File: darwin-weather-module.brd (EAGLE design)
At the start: 85 x 25 mm, 14 parts, among them U1 P82B715SOIC

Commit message: Schematic Cleanup
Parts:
- renumbered U$1 to J1, U$2 to U2, U$3 to U3, U$5 to J2
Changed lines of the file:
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@@
 </autorouter>
 <elements>
-<element name="U$1" library="Conservify" library_urn="urn:adsk.eagle:library:11839183" package="M20-7810645" package3d_urn="urn:adsk.eagle:package:11839232/3" value="2X6-HEADERS" x="7.5" y="12.5" smashed="yes" rot="R90"/>
-<element name="U$2" library="Conservify" library_urn="urn:adsk.eagle:library:11839183" package="QFN50P400X400X100-25T200" package3d_urn="urn:adsk.eagle:package:12019890/1" value="ATSAMD09" x="22" y="11" smashed="yes" rot="R270"/>
+<element name="J1" library="Conservify" library_urn="urn:adsk.eagle:library:11839183" package="M20-7810645" package3d_urn="urn:adsk.eagle:package:11839232/3" value="2X6-HEADERS" x="7.5" y="12.5" smashed="yes" rot="R90"/>
+<element name="U2" library="Conservify" library_urn="urn:adsk.eagle:library:11839183" package="QFN50P400X400X100-25T200" package3d_urn="urn:adsk.eagle:package:12019890/1" value="ATSAMD09" x="22" y="11" smashed="yes" rot="R270"/>
 <element name="U1" library="Conservify" library_urn="urn:adsk.eagle:library:11839183" package="SOIC127P599X175-8" package3d_urn="urn:adsk.eagle:package:11891718/1" value="P82B715SOIC" x="22" y="5" smashed="yes">
 <attribute name="NAME" x="22" y="8.5949" size="1.27" layer="25" align="bottom-center"/>
@@
 <attribute name="VALUE" x="26.9" y="17.6" size="0.4064" layer="27" ratio="10"/>
 </element>
-<element name="U$3" library="Conservify" library_urn="urn:adsk.eagle:library:11839183" package="SOIC127P600X175-8" package3d_urn="urn:adsk.eagle:package:12022475/1" value="M24C02-WMN6TP" x="15" y="5" smashed="yes" rot="R270"/>
-<element name="U$5" library="Conservify" library_urn="urn:adsk.eagle:library:11839183" package="85513-5009" package3d_urn="urn:adsk.eagle:package:12024212/2" value="95501-6889VERT" x="73" y="5" smashed="yes"/>
+<element name="U3" library="Conservify" library_urn="urn:adsk.eagle:library:11839183" package="SOIC127P600X175-8" package3d_urn="urn:adsk.eagle:package:12022475/1" value="M24C02-WMN6TP" x="15" y="5" smashed="yes" rot="R270"/>
+<element name="J2" library="Conservify" library_urn="urn:adsk.eagle:library:11839183" package="85513-5009" package3d_urn="urn:adsk.eagle:package:12024212/2" value="95501-6889VERT" x="73" y="5" smashed="yes"/>
 <element name="C1" library="rcl" library_urn="urn:adsk.eagle:library:334" package="C0603K" package3d_urn="urn:adsk.eagle:package:23680/2" value=".1uf" x="19" y="1.6" smashed="yes">
 <attribute name="NAME" x="20.867" y="1.107" size="1" layer="25" ratio="30"/>
@@
 <contactref element="X1" pad="5"/>
 <contactref element="X1" pad="9"/>
-<contactref element="U$2" pad="23"/>
+<contactref element="U2" pad="23"/>
 <contactref element="U1" pad="4"/>
 <wire x1="22.175" y1="18" x2="22.325" y2="18.15" width="0.1524" layer="1"/>
 <wire x1="22.325" y1="18.15" x2="24" y2="18.15" width="0.1524" layer="1"/>
-<contactref element="U$3" pad="1"/>
-<contactref element="U$3" pad="2"/>
-<contactref element="U$3" pad="3"/>
-<contactref element="U$3" pad="4"/>
+<contactref element="U3" pad="1"/>
+<contactref element="U3" pad="2"/>
+<contactref element="U3" pad="3"/>
+<contactref element="U3" pad="4"/>
 <polygon width="0.1524" layer="1">
 <vertex x="0" y="25"/>
@@
 <vertex x="0" y="0"/>
 </polygon>
-<contactref element="U$1" pad="P$8"/>
-<contactref element="U$5" pad="3"/>
-<contactref element="U$5" pad="2"/>
-<contactref element="U$5" pad="1"/>
+<contactref element="J1" pad="P$8"/>
+<contactref element="J2" pad="3"/>
+<contactref element="J2" pad="2"/>
+<contactref element="J2" pad="1"/>
 <polygon width="0.4064" layer="16">
 <vertex x="0" y="25"/>
@@
 <contactref element="C9" pad="1"/>
 <contactref element="X1" pad="1"/>
-<contactref element="U$2" pad="24"/>
+<contactref element="U2" pad="24"/>
 <contactref element="U1" pad="8"/>
 <wire x1="19.825" y1="17.05" x2="18.169" y2="17.05" width="0.1524" layer="1"/>
@@
 <wire x1="30.48" y1="15.875" x2="30.46" y2="15.895" width="0.1524" layer="1"/>
 <wire x1="30.46" y1="15.895" x2="30.46" y2="18.05" width="0.1524" layer="1"/>
-<contactref element="U$3" pad="8"/>
+<contactref element="U3" pad="8"/>
 <wire x1="26" y1="3.088459375" x2="26" y2="7" width="0.1524" layer="1"/>
 <wire x1="25.438140625" y1="2.5266" x2="26" y2="3.088459375" width="0.1524" layer="1"/>
@@
 <signal name="UNREG">
 <contactref element="U$4" pad="1"/>
-<contactref element="U$1" pad="P$7"/>
+<contactref element="J1" pad="P$7"/>
 <wire x1="4.59" y1="18.85" x2="4.59" y2="20.59" width="0.4064" layer="1"/>
 <wire x1="4.59" y1="20.59" x2="6" y2="22" width="0.4064" layer="1"/>
@@
 <wire x1="25" y1="16" x2="23.225" y2="16" width="0.4064" layer="1"/>
 <wire x1="23.225" y1="16" x2="22.175" y2="17.05" width="0.4064" layer="1"/>
-<contactref element="U$5" pad="4"/>
-<contactref element="U$5" pad="5"/>
-<contactref element="U$5" pad="6"/>
+<contactref element="J2" pad="4"/>
+<contactref element="J2" pad="5"/>
+<contactref element="J2" pad="6"/>
 <wire x1="24" y1="22" x2="28.42710625" y2="22" width="0.4064" layer="1"/>
 <wire x1="28.42710625" y1="22" x2="29.93270625" y2="23.5056" width="0.4064" layer="1"/>
@@
 <signal name="SWCLK">
 <contactref element="X1" pad="4"/>
-<contactref element="U$2" pad="19"/>
+<contactref element="U2" pad="19"/>
 <wire x1="31.73" y1="21.27" x2="31.73" y2="21.95" width="0.1524" layer="1"/>
 <wire x1="29.004271875" y1="18.544271875" x2="31.73" y2="21.27" width="0.1524" layer="1"/>
@@
 <signal name="SWDIO">
 <contactref element="X1" pad="2"/>
-<contactref element="U$2" pad="20"/>
+<contactref element="U2" pad="20"/>
 <wire x1="27.469375" y1="18.959375" x2="30.46" y2="21.95" width="0.1524" layer="1"/>
 <wire x1="27.469375" y1="13.484196875" x2="27.469375" y2="18.959375" width="0.1524" layer="1"/>
@@
 <signal name="RESET">
 <contactref element="X1" pad="10"/>
-<contactref element="U$2" pad="18"/>
+<contactref element="U2" pad="18"/>
 <wire x1="35.54" y1="21.27" x2="35.54" y2="21.95" width="0.1524" layer="1"/>
 <wire x1="33.635" y1="19.365" x2="35.54" y2="21.27" width="0.1524" layer="1"/>
@@
 </signal>
 <signal name="SDA">
-<contactref element="U$2" pad="11"/>
-<contactref element="U$3" pad="5"/>
+<contactref element="U2" pad="11"/>
+<contactref element="U3" pad="5"/>
 <wire x1="19.764834375" y1="10.25" x2="20.0627" y2="10.25" width="0.1524" layer="1"/>
 <wire x1="17.8350375" y1="8.320203125" x2="19.764834375" y2="10.25" width="0.1524" layer="1"/>
@@
 <wire x1="13.095" y1="2.782034375" x2="15.312965625" y2="5" width="0.1524" layer="1"/>
 <wire x1="13.095" y1="2.5266" x2="13.095" y2="2.782034375" width="0.1524" layer="1"/>
-<contactref element="U$1" pad="P$3"/>
+<contactref element="J1" pad="P$3"/>
 <wire x1="10.41" y1="11.23" x2="12.58185" y2="9.05815" width="0.1524" layer="1"/>
 <wire x1="13.095" y1="5.9479875" x2="13.095" y2="2.5266" width="0.1524" layer="1"/>
@@
 </signal>
 <signal name="SCL">
-<contactref element="U$2" pad="12"/>
-<contactref element="U$3" pad="6"/>
+<contactref element="U2" pad="12"/>
+<contactref element="U3" pad="6"/>
 <wire x1="18.19111875" y1="7.87841875" x2="20.0627" y2="9.75" width="0.1524" layer="1"/>
 <wire x1="18.19111875" y1="6.759465625" x2="18.19111875" y2="7.87841875" width="0.1524" layer="1"/>
 <wire x1="14.365" y1="2.933346875" x2="18.19111875" y2="6.759465625" width="0.1524" layer="1"/>
 <wire x1="14.365" y1="2.5266" x2="14.365" y2="2.933346875" width="0.1524" layer="1"/>
-<contactref element="U$1" pad="P$2"/>
+<contactref element="J1" pad="P$2"/>
 <wire x1="10.41" y1="8.69" x2="12.27705" y2="6.82295" width="0.1524" layer="1"/>
 <wire x1="13" y1="1.0961875" x2="13" y2="1.0922" width="0.1524" layer="1"/>
@@
 </signal>
 <signal name="SENSE-SDA">
-<contactref element="U$2" pad="15"/>
+<contactref element="U2" pad="15"/>
 <contactref element="U1" pad="3"/>
 <wire x1="19.5299" y1="4.365" x2="20.796340625" y2="4.365" width="0.1524" layer="1"/>
@@
 </signal>
 <signal name="SENSE-SCL">
-<contactref element="U$2" pad="16"/>
+<contactref element="U2" pad="16"/>
 <contactref element="U1" pad="6"/>
 <wire x1="24.4701" y1="4.365" x2="23.203659375" y2="4.365" width="0.1524" layer="1"/>
@@
 </signal>
 <signal name="WC">
-<contactref element="U$2" pad="13"/>
-<contactref element="U$3" pad="7"/>
+<contactref element="U2" pad="13"/>
+<contactref element="U3" pad="7"/>
 <wire x1="20.75" y1="6.588659375" x2="20.75" y2="9.0627" width="0.1524" layer="1"/>
 <wire x1="20.4737875" y1="6.312446875" x2="20.75" y2="6.588659375" width="0.1524" layer="1"/>
@@
 </signal>
 <signal name="NC">
-<contactref element="U$1" pad="P$1"/>
+<contactref element="J1" pad="P$1"/>
 </signal>
 <signal name="MISO">
-<contactref element="U$1" pad="P$4"/>
+<contactref element="J1" pad="P$4"/>
 </signal>
 <signal name="MOSI">
-<contactref element="U$1" pad="P$5"/>
+<contactref element="J1" pad="P$5"/>
 </signal>
 <signal name="SCK">
-<contactref element="U$1" pad="P$6"/>
+<contactref element="J1" pad="P$6"/>
 </signal>
 <signal name="ENABLE">
-<contactref element="U$1" pad="P$10"/>
+<contactref element="J1" pad="P$10"/>
 <contactref element="U$4" pad="3"/>
 <contactref element="R1" pad="2"/>
@@
 </signal>
 <signal name="G1">
-<contactref element="U$1" pad="P$11"/>
+<contactref element="J1" pad="P$11"/>
 </signal>
 <signal name="G2">
-<contactref element="U$1" pad="P$12"/>
+<contactref element="J1" pad="P$12"/>
 </signal>
 <signal name="IN3V3">
-<contactref element="U$1" pad="P$9"/>
+<contactref element="J1" pad="P$9"/>
 </signal>
 <signal name="LCL">
-<contactref element="U$5" pad="7"/>
+<contactref element="J2" pad="7"/>
 <contactref element="U1" pad="7"/>
 <wire x1="24.4701" y1="5.635" x2="23.6068" y2="5.635" width="0.1524" layer="1"/>
@@
 </signal>
 <signal name="LDA">
-<contactref element="U$5" pad="8"/>
+<contactref element="J2" pad="8"/>
 <contactref element="U1" pad="2"/>
 <wire x1="19.5299" y1="5.635" x2="21.127" y2="5.635" width="0.1524" layer="1"/>

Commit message: Added I2C Pullups and GPIO connection to backplane. Removed deprecated module mounting hole.
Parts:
- added R2, R3: 4.7k, SparkFun-Resistors:0603
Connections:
- net 3V3: now also R2.1, R3.1
- net G1: now also U2.22
- net SCL: now also R3.2
- net SDA: now also R2.2
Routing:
- net G1: track 0.00 -> 32.3 mm, vias 0 -> 2
- net 3V3: track 49.8 -> 68.1 mm, vias 3 -> 5
- net SDA: track 21.0 -> 23.3 mm
- net GND: track 1.89 -> 3.30 mm
- net SCL: track 20.8 -> 22.1 mm
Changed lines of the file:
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@@
 <attribute name="SPICEPREFIX" value="C" x="25.4" y="14.4" size="1.778" layer="27" display="off"/>
+</element>
+<element name="R2" library="SparkFun-Resistors" library_urn="urn:adsk.eagle:library:532" package="0603" package3d_urn="urn:adsk.eagle:package:39650/1" value="4.7k" x="13.6" y="11.2" smashed="yes" rot="R180">
+<attribute name="NAME" x="13.6" y="10.438" size="0.6096" layer="25" font="vector" ratio="20" rot="R180" align="bottom-center"/>
+<attribute name="PROD_ID" value="RES-07828" x="13.6" y="11.2" size="1.778" layer="27" rot="R180" display="off"/>
+<attribute name="VALUE" x="13.6" y="11.962" size="0.6096" layer="27" font="vector" ratio="20" rot="R180" align="top-center"/>
+</element>
+<element name="R3" library="SparkFun-Resistors" library_urn="urn:adsk.eagle:library:532" package="0603" package3d_urn="urn:adsk.eagle:package:39650/1" value="4.7k" x="10.4" y="2.4" smashed="yes">
+<attribute name="NAME" x="10.4" y="3.162" size="0.6096" layer="25" font="vector" ratio="20" align="bottom-center"/>
+<attribute name="PROD_ID" value="RES-07828" x="10.4" y="2.4" size="1.778" layer="27" display="off"/>
+<attribute name="VALUE" x="10.4" y="1.638" size="0.6096" layer="27" font="vector" ratio="20" align="top-center"/>
 </element>
 </elements>
 <signals>
 <signal name="N$1">
-<via x="33.5" y="12.5" extent="1-16" drill="4.2" diameter="6"/>
 <via x="58.5" y="12.5" extent="1-16" drill="4.2" diameter="6"/>
-<wire x1="33.5" y1="12.5" x2="58.5" y2="12.5" width="0" layer="19" extent="1-1"/>
 </signal>
 <signal name="GND">
@@
 <via x="25.2" y="1.6" extent="1-16" drill="0.35"/>
 <via x="26.2" y="1.6" extent="1-16" drill="0.35"/>
+<wire x1="24.48515625" y1="11.8" x2="23.9873" y2="11.8" width="0.1524" layer="1"/>
+<wire x1="23.9373" y1="11.75" x2="23.9873" y2="11.8" width="0.1524" layer="1"/>
+<wire x1="24.48515625" y1="11.8" x2="24.6" y2="11.91484375" width="0.1524" layer="1"/>
+<wire x1="24.6" y1="11.91484375" x2="24.6" y2="12.6" width="0.1524" layer="1"/>
 </signal>
 <signal name="3V3">
@@
 <wire x1="24.5651" y1="7" x2="26" y2="7" width="0.1524" layer="1"/>
 <via x="26" y="7" extent="1-16" drill="0.35"/>
-<wire x1="26" y1="7" x2="22" y2="11" width="0.1524" layer="16"/>
-<wire x1="22" y1="11" x2="22" y2="15" width="0.1524" layer="16"/>
+<wire x1="26" y1="12.4" x2="26" y2="7" width="0.1524" layer="16"/>
+<wire x1="26" y1="12.4" x2="23.4" y2="15" width="0.1524" layer="16"/>
+<wire x1="23.4" y1="15" x2="22" y2="15" width="0.1524" layer="16"/>
 <via x="22" y="15" extent="1-16" drill="0.35"/>
 <wire x1="22" y1="15" x2="22.875" y2="15.875" width="0.1524" layer="16"/>
@@
 <wire x1="26" y1="3.088459375" x2="26" y2="7" width="0.1524" layer="1"/>
 <wire x1="25.438140625" y1="2.5266" x2="26" y2="3.088459375" width="0.1524" layer="1"/>
-<wire x1="16.905" y1="2.5266" x2="17" y2="2.5266" width="0.1524" layer="1"/>
 <contactref element="C2" pad="1"/>
 <contactref element="C1" pad="1"/>
 <contactref element="C3" pad="1"/>
-<wire x1="17.1984" y1="2.5266" x2="25.438140625" y2="2.5266" width="0.1524" layer="1"/>
+<wire x1="17.1984" y1="2.5266" x2="18" y2="2.5266" width="0.1524" layer="1"/>
+<wire x1="18" y1="2.5266" x2="25.438140625" y2="2.5266" width="0.1524" layer="1"/>
 <wire x1="24.525" y1="14.4" x2="23.9373" y2="13.8123" width="0.1524" layer="1"/>
 <wire x1="23.9373" y1="13.8123" x2="23.9373" y2="13.0627" width="0.1524" layer="1"/>
@@
 <wire x1="27.125" y1="7" x2="26" y2="7" width="0.1524" layer="1"/>
 <wire x1="18.125" y1="1.6" x2="17.1984" y2="2.5266" width="0.1524" layer="1"/>
-<wire x1="17.1984" y1="2.5266" x2="17" y2="2.5266" width="0.1524" layer="1"/>
+<wire x1="17.1984" y1="2.5266" x2="16.905" y2="2.5266" width="0.1524" layer="1"/>
+<contactref element="R3" pad="1"/>
+<contactref element="R2" pad="1"/>
+<wire x1="14.45" y1="11.2" x2="14.45" y2="14.518" width="0.1524" layer="1"/>
+<wire x1="14.45" y1="14.518" x2="16.539" y2="16.607" width="0.1524" layer="1"/>
+<wire x1="9.55" y1="2.4" x2="8.2" y2="2.4" width="0.1524" layer="1"/>
+<via x="8.2" y="2.4" extent="1-16" drill="0.35"/>
+<wire x1="8.2" y1="2.4" x2="17.8734" y2="2.4" width="0.1524" layer="16"/>
+<wire x1="17.8734" y1="2.4" x2="18" y2="2.5266" width="0.1524" layer="16"/>
+<via x="18" y="2.5266" extent="1-16" drill="0.35"/>
 </signal>
 <signal name="N$6">
@@
 <wire x1="31.73" y1="21.27" x2="31.73" y2="21.95" width="0.1524" layer="1"/>
 <wire x1="29.004271875" y1="18.544271875" x2="31.73" y2="21.27" width="0.1524" layer="1"/>
-<wire x1="29.004271875" y1="14.51909375" x2="29.004271875" y2="18.544271875" width="0.1524" layer="1"/>
-<wire x1="24.235178125" y1="9.75" x2="29.004271875" y2="14.51909375" width="0.1524" layer="1"/>
-<wire x1="23.9373" y1="9.75" x2="24.235178125" y2="9.75" width="0.1524" layer="1"/>
+<wire x1="29.004271875" y1="14.11909375" x2="29.004271875" y2="18.544271875" width="0.1524" layer="1"/>
+<wire x1="24.635178125" y1="9.75" x2="29.004271875" y2="14.11909375" width="0.1524" layer="1"/>
+<wire x1="23.9373" y1="9.75" x2="24.635178125" y2="9.75" width="0.1524" layer="1"/>
 </signal>
 <signal name="SWDIO">
@@
 <contactref element="U2" pad="20"/>
 <wire x1="27.469375" y1="18.959375" x2="30.46" y2="21.95" width="0.1524" layer="1"/>
-<wire x1="27.469375" y1="13.484196875" x2="27.469375" y2="18.959375" width="0.1524" layer="1"/>
-<wire x1="24.235178125" y1="10.25" x2="27.469375" y2="13.484196875" width="0.1524" layer="1"/>
-<wire x1="23.9373" y1="10.25" x2="24.235178125" y2="10.25" width="0.1524" layer="1"/>
+<wire x1="27.469375" y1="13.084196875" x2="27.469375" y2="18.959375" width="0.1524" layer="1"/>
+<wire x1="24.635178125" y1="10.25" x2="27.469375" y2="13.084196875" width="0.1524" layer="1"/>
+<wire x1="23.9373" y1="10.25" x2="24.635178125" y2="10.25" width="0.1524" layer="1"/>
 </signal>
 <signal name="RESET">
@@
 <wire x1="13.095" y1="2.5266" x2="13.095" y2="2.782034375" width="0.1524" layer="1"/>
 <contactref element="J1" pad="P$3"/>
-<wire x1="10.41" y1="11.23" x2="12.58185" y2="9.05815" width="0.1524" layer="1"/>
 <wire x1="13.095" y1="5.9479875" x2="13.095" y2="2.5266" width="0.1524" layer="1"/>
 <wire x1="12.58185" y1="9.05815" x2="12.58185" y2="6.4611375" width="0.1524" layer="1"/>
 <wire x1="12.58185" y1="6.4611375" x2="13.095" y2="5.9479875" width="0.1524" layer="1"/>
+<contactref element="R2" pad="2"/>
+<wire x1="10.41" y1="11.23" x2="12.58185" y2="9.05815" width="0.1524" layer="1"/>
+<wire x1="10.41" y1="11.23" x2="12.72" y2="11.23" width="0.1524" layer="1"/>
+<wire x1="12.72" y1="11.23" x2="12.75" y2="11.2" width="0.1524" layer="1"/>
 </signal>
 <signal name="SCL">
@@
 <contactref element="J1" pad="P$2"/>
 <wire x1="10.41" y1="8.69" x2="12.27705" y2="6.82295" width="0.1524" layer="1"/>
-<wire x1="13" y1="1.0961875" x2="13" y2="1.0922" width="0.1524" layer="1"/>
-<wire x1="12.27705" y1="6.82295" x2="12.27705" y2="1.8191375" width="0.1524" layer="1"/>
-<wire x1="12.27705" y1="1.8191375" x2="13" y2="1.0961875" width="0.1524" layer="1"/>
-<wire x1="13" y1="1.0922" x2="14" y2="1.0922" width="0.1524" layer="1"/>
+<wire x1="12.6" y1="1.0961875" x2="12.6" y2="1.0922" width="0.1524" layer="1"/>
+<wire x1="12.27705" y1="6.82295" x2="12.27705" y2="2.4191375" width="0.1524" layer="1"/>
+<wire x1="12.27705" y1="2.4191375" x2="12.27705" y2="1.4191375" width="0.1524" layer="1"/>
+<wire x1="12.27705" y1="1.4191375" x2="12.6" y2="1.0961875" width="0.1524" layer="1"/>
+<wire x1="12.6" y1="1.0922" x2="14" y2="1.0922" width="0.1524" layer="1"/>
 <wire x1="14" y1="1.0922" x2="14.365" y2="1.4572" width="0.1524" layer="1"/>
 <wire x1="14.365" y1="1.4572" x2="14.365" y2="2.5266" width="0.1524" layer="1"/>
+<contactref element="R3" pad="2"/>
+<wire x1="11.25" y1="2.4" x2="12.2579125" y2="2.4" width="0.1524" layer="1"/>
+<wire x1="12.2579125" y1="2.4" x2="12.27705" y2="2.4191375" width="0.1524" layer="1"/>
 </signal>
 <signal name="SENSE-SDA">
@@
 <signal name="G1">
 <contactref element="J1" pad="P$11"/>
+<contactref element="U2" pad="22"/>
+<wire x1="4.59" y1="8.69" x2="3.09" y2="8.69" width="0.1524" layer="1"/>
+<wire x1="3.09" y1="8.69" x2="2.2" y2="7.8" width="0.1524" layer="1"/>
+<via x="2.2" y="7.8" extent="1-16" drill="0.35"/>
+<wire x1="2.2" y1="7.8" x2="2.31414375" y2="7.8" width="0.1524" layer="16"/>
+<wire x1="2.31414375" y1="7.8" x2="5.56634375" y2="4.5478" width="0.1524" layer="16"/>
+<wire x1="5.56634375" y1="4.5478" x2="18.1478" y2="4.5478" width="0.1524" layer="16"/>
+<wire x1="25.363515625" y1="11.763515625" x2="25.363515625" y2="12.0364875" width="0.1524" layer="16"/>
+<via x="25.363515625" y="12.0364875" extent="1-16" drill="0.35"/>
+<wire x1="25.363515625" y1="12.0364875" x2="24.577028125" y2="11.25" width="0.1524" layer="1"/>
+<wire x1="24.577028125" y1="11.25" x2="23.9373" y2="11.25" width="0.1524" layer="1"/>
+<wire x1="18.1478" y1="4.5478" x2="25.363515625" y2="11.763515625" width="0.1524" layer="16"/>
 </signal>
 <signal name="G2">

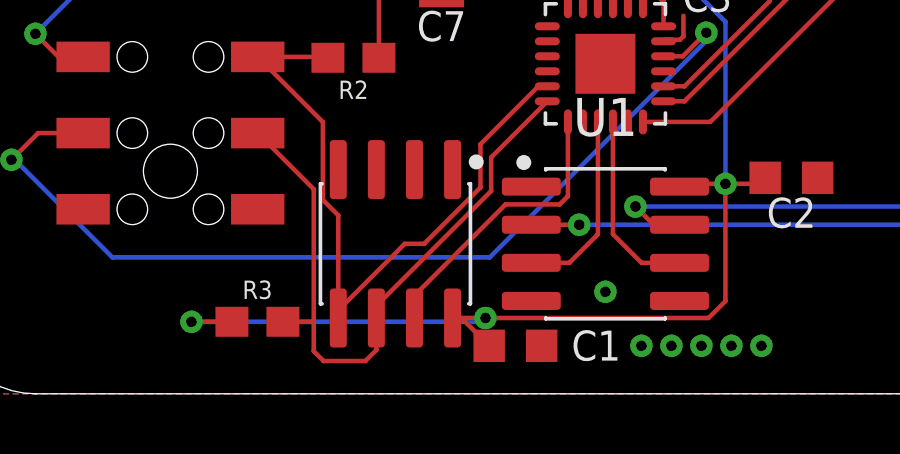
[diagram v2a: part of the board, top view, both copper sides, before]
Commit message: Fixed via overlap. TA2.
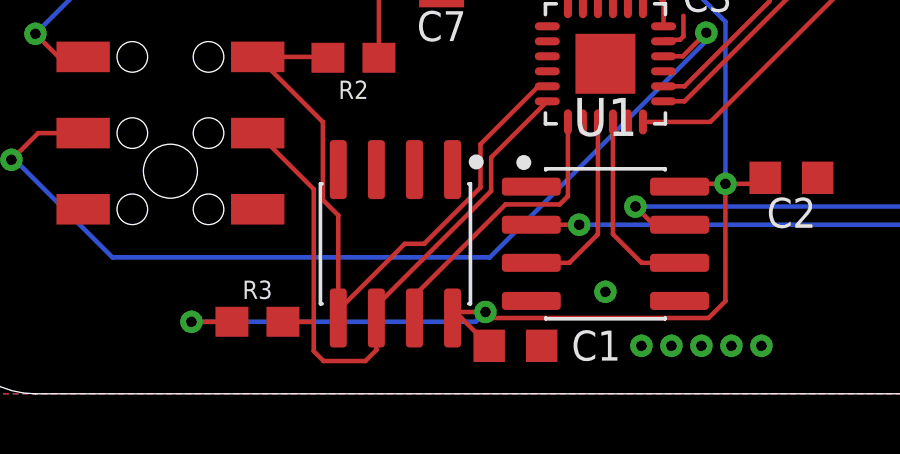
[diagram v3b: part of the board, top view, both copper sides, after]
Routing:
- net 3V3: track 68.1 -> 68.8 mm
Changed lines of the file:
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@@
 <contactref element="C1" pad="1"/>
 <contactref element="C3" pad="1"/>
-<wire x1="17.1984" y1="2.5266" x2="18" y2="2.5266" width="0.1524" layer="1"/>
-<wire x1="18" y1="2.5266" x2="25.438140625" y2="2.5266" width="0.1524" layer="1"/>
+<wire x1="16.9984" y1="2.7266" x2="18" y2="2.7266" width="0.1524" layer="1"/>
+<wire x1="18" y1="2.7266" x2="18.2" y2="2.5266" width="0.1524" layer="1"/>
+<wire x1="25.438140625" y1="2.5266" x2="18.2" y2="2.5266" width="0.1524" layer="1"/>
 <wire x1="24.525" y1="14.4" x2="23.9373" y2="13.8123" width="0.1524" layer="1"/>
 <wire x1="23.9373" y1="13.8123" x2="23.9373" y2="13.0627" width="0.1524" layer="1"/>
@@
 <wire x1="27.125" y1="7" x2="26" y2="7" width="0.1524" layer="1"/>
 <wire x1="18.125" y1="1.6" x2="17.1984" y2="2.5266" width="0.1524" layer="1"/>
+<wire x1="17.1984" y1="2.5266" x2="16.9984" y2="2.7266" width="0.1524" layer="1"/>
 <wire x1="17.1984" y1="2.5266" x2="16.905" y2="2.5266" width="0.1524" layer="1"/>
 <contactref element="R3" pad="1"/>
@@
 <wire x1="9.55" y1="2.4" x2="8.2" y2="2.4" width="0.1524" layer="1"/>
 <via x="8.2" y="2.4" extent="1-16" drill="0.35"/>
-<wire x1="8.2" y1="2.4" x2="17.8734" y2="2.4" width="0.1524" layer="16"/>
-<wire x1="17.8734" y1="2.4" x2="18" y2="2.5266" width="0.1524" layer="16"/>
-<via x="18" y="2.5266" extent="1-16" drill="0.35"/>
+<wire x1="8.2" y1="2.4" x2="17.6734" y2="2.4" width="0.1524" layer="16"/>
+<wire x1="17.6734" y1="2.4" x2="18" y2="2.7266" width="0.1524" layer="16"/>
+<via x="18" y="2.7266" extent="1-16" drill="0.35"/>
 </signal>
 <signal name="N$6">
